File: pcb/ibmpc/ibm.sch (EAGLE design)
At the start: 40 parts, among them J2 ATX24RH

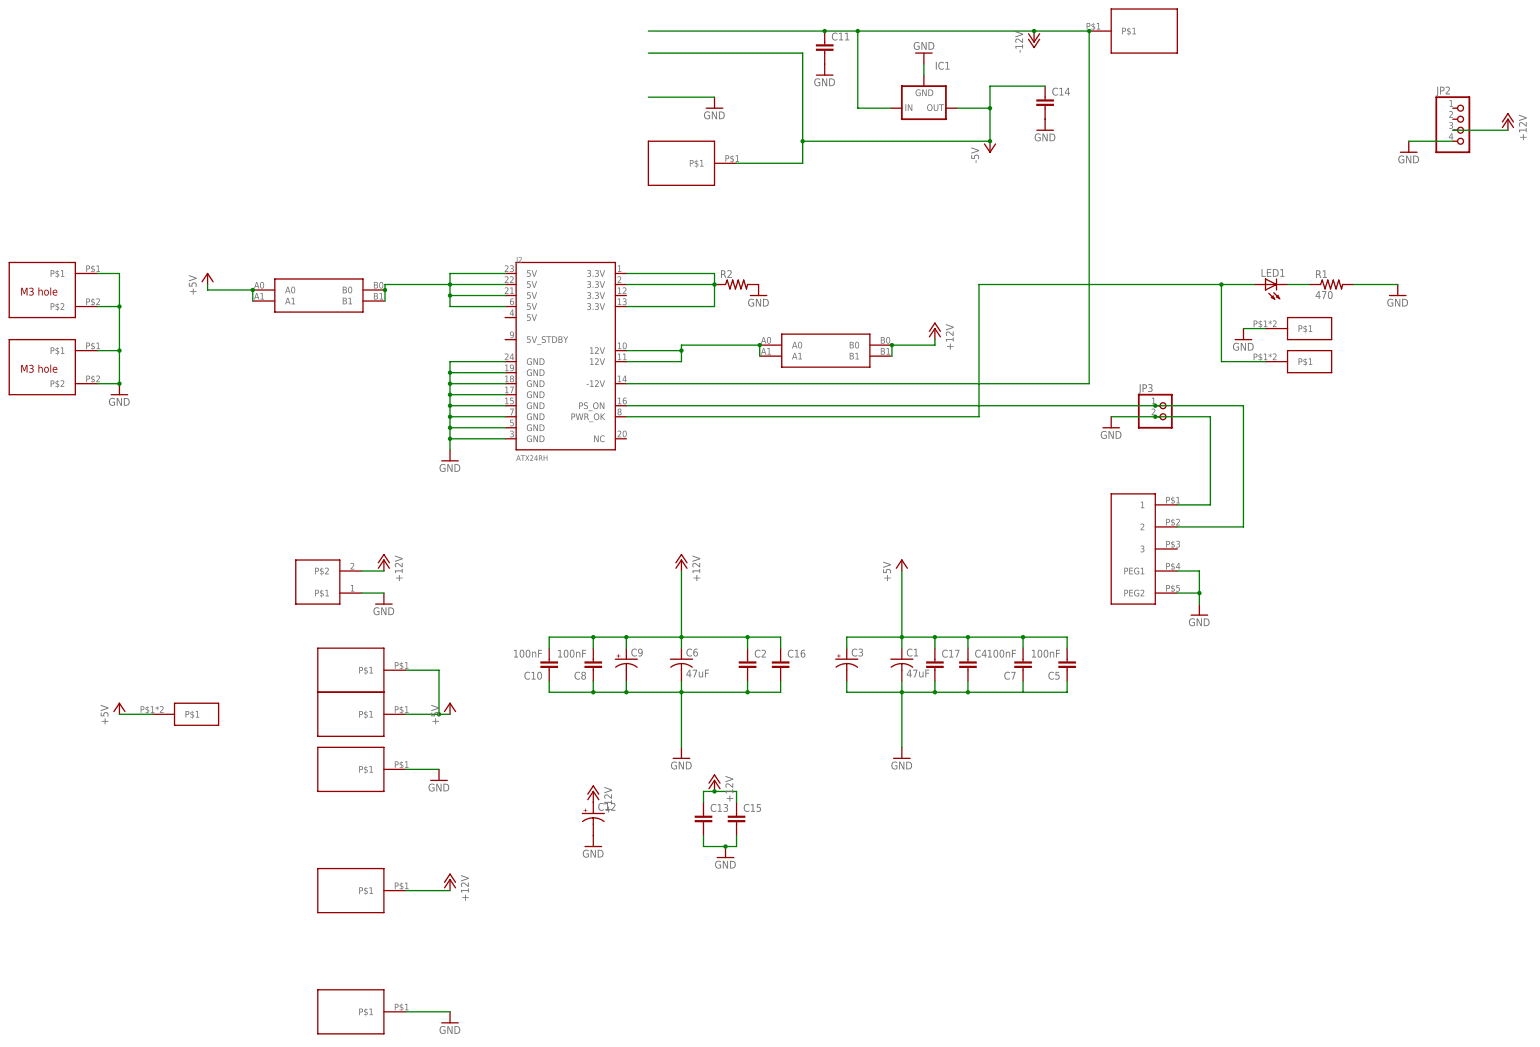
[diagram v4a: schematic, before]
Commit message: added 12V load resistor and blade
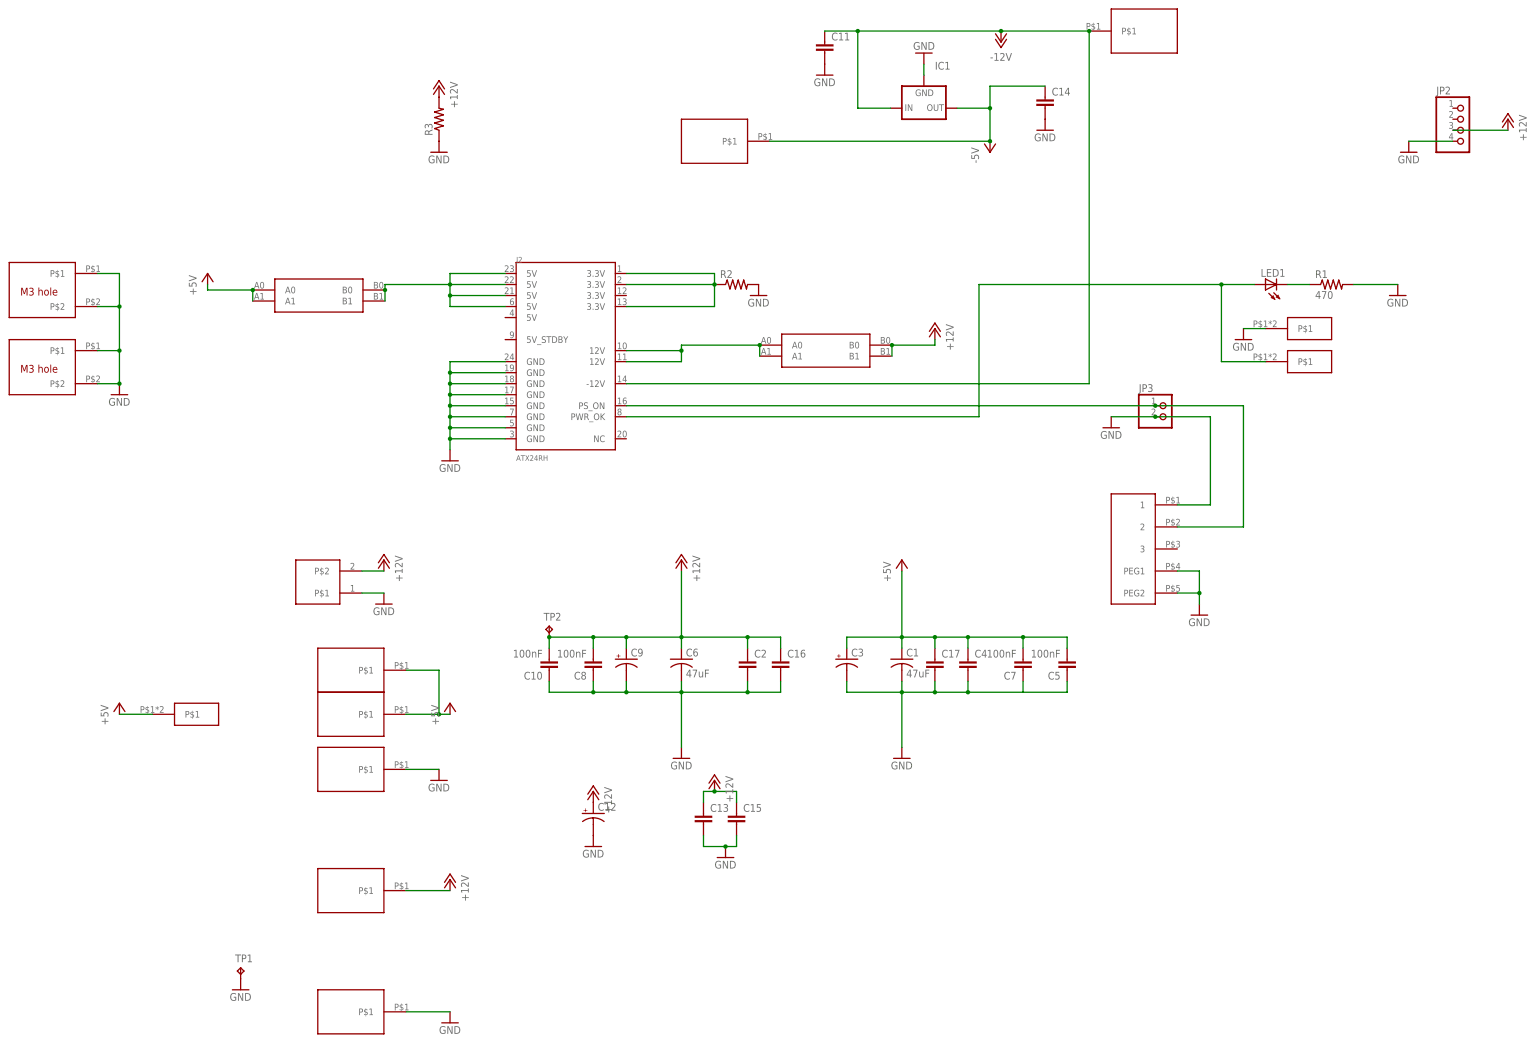
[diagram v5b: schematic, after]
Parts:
- added R3: (no value), adafruit_changed:R-US_0411/15
- added TP1, TP2: TPPAD1-13, testpad:TPPAD1-13
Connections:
- net +12V: now also R3.2, TP2.TP
- net GND: now also R3.1, TP1.TP
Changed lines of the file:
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@@
 <part name="C8" library="clock" deviceset="CAP" device="0805" value="100nF"/>
 <part name="C10" library="clock" deviceset="CAP" device="0805" value="100nF"/>
-<part name="GND5" library="supply1" library_urn="urn:adsk.eagle:library:371" deviceset="GND" device=""/>
 <part name="GND7" library="supply1" library_urn="urn:adsk.eagle:library:371" deviceset="GND" device=""/>
 <part name="C14" library="capacitor-wima" library_urn="urn:adsk.eagle:library:116" deviceset="C" device="5/2.5" package3d_urn="urn:adsk.eagle:package:5426/1"/>
@@
 <part name="P+9" library="supply1" library_urn="urn:adsk.eagle:library:371" deviceset="+12V" device=""/>
 <part name="GND19" library="supply1" library_urn="urn:adsk.eagle:library:371" deviceset="GND" device=""/>
+<part name="R3" library="adafruit_changed" deviceset="R-US_" device="0411/15"/>
+<part name="GND5" library="supply1" library_urn="urn:adsk.eagle:library:371" deviceset="GND" device=""/>
+<part name="P+12" library="supply1" library_urn="urn:adsk.eagle:library:371" deviceset="+12V" device=""/>
+<part name="TP2" library="testpad" library_urn="urn:adsk.eagle:library:385" deviceset="TP" device="PAD1-13" package3d_urn="urn:adsk.eagle:package:27946/1"/>
+<part name="TP1" library="testpad" library_urn="urn:adsk.eagle:library:385" deviceset="TP" device="PAD1-13" package3d_urn="urn:adsk.eagle:package:27946/1"/>
+<part name="GND20" library="supply1" library_urn="urn:adsk.eagle:library:371" deviceset="GND" device=""/>
 </parts>
 <sheets>
@@
 <attribute name="VALUE" x="89.916" y="106.299" size="1.778" layer="96" rot="R180"/>
 </instance>
-<instance part="GND5" gate="1" x="129.54" y="231.14" smashed="yes">
-<attribute name="VALUE" x="127" y="228.6" size="1.778" layer="96"/>
-</instance>
 <instance part="GND7" gate="1" x="177.8" y="243.84" smashed="yes" rot="R180">
 <attribute name="VALUE" x="180.34" y="246.38" size="1.778" layer="96" rot="R180"/>
@@
 <attribute name="VALUE" x="181.864" y="99.441" size="1.778" layer="96"/>
 </instance>
-<instance part="U$7" gate="G$1" x="121.92" y="218.44" smashed="yes"/>
+<instance part="U$7" gate="G$1" x="129.54" y="223.52" smashed="yes"/>
 <instance part="U$9" gate="G$1" x="45.72" y="22.86" smashed="yes"/>
 <instance part="GND14" gate="1" x="68.58" y="20.32" smashed="yes">
@@
 <attribute name="VALUE" x="152.4" y="236.22" size="1.778" layer="96"/>
 </instance>
-<instance part="P-1" gate="1" x="203.2" y="246.38" smashed="yes">
-<attribute name="VALUE" x="200.66" y="243.84" size="1.778" layer="96" rot="R90"/>
+<instance part="P-1" gate="1" x="195.58" y="246.38" smashed="yes">
+<attribute name="VALUE" x="198.12" y="243.84" size="1.778" layer="96" rot="R180"/>
 </instance>
 <instance part="P-2" gate="1" x="193.04" y="220.98" smashed="yes">
@@
 <instance part="GND19" gate="1" x="132.08" y="58.42" smashed="yes">
 <attribute name="VALUE" x="129.54" y="55.88" size="1.778" layer="96"/>
+</instance>
+<instance part="R3" gate="G$1" x="66.04" y="228.6" smashed="yes" rot="R90">
+<attribute name="NAME" x="64.5414" y="224.79" size="1.778" layer="95" rot="R90"/>
+<attribute name="VALUE" x="69.342" y="224.79" size="1.778" layer="96" rot="R90"/>
+</instance>
+<instance part="GND5" gate="1" x="66.04" y="220.98" smashed="yes">
+<attribute name="VALUE" x="63.5" y="218.44" size="1.778" layer="96"/>
+</instance>
+<instance part="P+12" gate="1" x="66.04" y="236.22" smashed="yes" rot="MR0">
+<attribute name="VALUE" x="68.58" y="231.14" size="1.778" layer="96" rot="MR90"/>
+</instance>
+<instance part="TP2" gate="G$1" x="91.44" y="111.76" smashed="yes">
+<attribute name="NAME" x="90.17" y="113.03" size="1.778" layer="95"/>
+<attribute name="TP_SIGNAL_NAME" x="92.71" y="110.49" size="1.778" layer="97"/>
+</instance>
+<instance part="TP1" gate="G$1" x="20.32" y="33.02" smashed="yes">
+<attribute name="NAME" x="19.05" y="34.29" size="1.778" layer="95"/>
+<attribute name="TP_SIGNAL_NAME" x="21.59" y="31.75" size="1.778" layer="97"/>
+</instance>
+<instance part="GND20" gate="1" x="20.32" y="27.94" smashed="yes">
+<attribute name="VALUE" x="17.78" y="25.4" size="1.778" layer="96"/>
 </instance>
 </instances>
@@
 </segment>
 <segment>
-<pinref part="GND5" gate="1" pin="GND"/>
-<wire x1="114.3" y1="233.68" x2="129.54" y2="233.68" width="0.1524" layer="91"/>
-</segment>
-<segment>
 <pinref part="C14" gate="G$1" pin="2"/>
 <pinref part="GND8" gate="1" pin="GND"/>
@@
 <pinref part="U$14" gate="G$1" pin="P$1"/>
 <wire x1="251.46" y1="180.34" x2="256.54" y2="180.34" width="0.1524" layer="91"/>
+</segment>
+<segment>
+<pinref part="R3" gate="G$1" pin="1"/>
+<pinref part="GND5" gate="1" pin="GND"/>
+</segment>
+<segment>
+<pinref part="TP1" gate="G$1" pin="TP"/>
+<pinref part="GND20" gate="1" pin="GND"/>
 </segment>
 </net>
@@
 <wire x1="144.78" y1="109.22" x2="144.78" y2="106.68" width="0.1524" layer="91"/>
 <junction x="137.16" y="109.22"/>
+<pinref part="TP2" gate="G$1" pin="TP"/>
+<junction x="91.44" y="109.22"/>
 </segment>
 <segment>
@@
 <junction x="129.54" y="73.66"/>
 </segment>
+<segment>
+<pinref part="R3" gate="G$1" pin="2"/>
+<pinref part="P+12" gate="1" pin="+12V"/>
+</segment>
 </net>
 <net name="-12V" class="0">
@@
 <wire x1="109.22" y1="167.64" x2="215.9" y2="167.64" width="0.1524" layer="91"/>
 <wire x1="215.9" y1="167.64" x2="215.9" y2="248.92" width="0.1524" layer="91"/>
-<wire x1="215.9" y1="248.92" x2="203.2" y2="248.92" width="0.1524" layer="91"/>
-<wire x1="203.2" y1="248.92" x2="162.56" y2="248.92" width="0.1524" layer="91"/>
+<wire x1="215.9" y1="248.92" x2="195.58" y2="248.92" width="0.1524" layer="91"/>
+<wire x1="195.58" y1="248.92" x2="162.56" y2="248.92" width="0.1524" layer="91"/>
 <wire x1="162.56" y1="248.92" x2="154.94" y2="248.92" width="0.1524" layer="91"/>
-<wire x1="154.94" y1="248.92" x2="114.3" y2="248.92" width="0.1524" layer="91"/>
 <wire x1="162.56" y1="231.14" x2="162.56" y2="248.92" width="0.1524" layer="91"/>
 <junction x="162.56" y="248.92"/>
@@
 <junction x="215.9" y="248.92"/>
 <pinref part="C11" gate="G$1" pin="1"/>
-<junction x="154.94" y="248.92"/>
 <pinref part="P-1" gate="1" pin="-12V"/>
-<junction x="203.2" y="248.92"/>
+<junction x="195.58" y="248.92"/>
 </segment>
 </net>
@@
 <net name="-5V" class="0">
 <segment>
-<wire x1="193.04" y1="223.52" x2="149.86" y2="223.52" width="0.1524" layer="91"/>
-<wire x1="149.86" y1="223.52" x2="149.86" y2="243.84" width="0.1524" layer="91"/>
+<wire x1="193.04" y1="223.52" x2="142.24" y2="223.52" width="0.1524" layer="91"/>
 <pinref part="C14" gate="G$1" pin="1"/>
-<wire x1="149.86" y1="243.84" x2="114.3" y2="243.84" width="0.1524" layer="91"/>
 <wire x1="193.04" y1="236.22" x2="205.74" y2="236.22" width="0.1524" layer="91"/>
 <wire x1="185.42" y1="231.14" x2="193.04" y2="231.14" width="0.1524" layer="91"/>
@@
 <pinref part="IC1" gate="1" pin="OUT"/>
 <pinref part="U$7" gate="G$1" pin="P$1"/>
-<wire x1="134.62" y1="218.44" x2="149.86" y2="218.44" width="0.1524" layer="91"/>
-<wire x1="149.86" y1="218.44" x2="149.86" y2="223.52" width="0.1524" layer="91"/>
-<junction x="149.86" y="223.52"/>
 <pinref part="P-2" gate="1" pin="-5V"/>
 <junction x="193.04" y="223.52"/>
